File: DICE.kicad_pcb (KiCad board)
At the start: 2 copper layers, 117.3 x 128.5 mm, 116 parts, among them J101 Conn_01x03_Pin, J102 AudioJack2, J103 AudioJack2, J104 AudioJack2, J105 AudioJack2, J106 AudioJack2, J107 AudioJack2, J108 Conn_02x05_Odd_Even, J109 Conn_01x03_Pin, J11 AudioJack2, J110 Conn_01x05_Pin, J111 Conn_01x05_Pin, J112 Conn_01x07_Pin, J113 Conn_01x07_Pin, J114 Conn_01x07_Pin, J115 Conn_01x07_Pin, J116 Conn_01x03_Pin, J117 Conn_01x03_Pin, J2 Conn_01x03_Pin, Q101 BC847, Q102 BC847, SW1 SW_SPDT, SW101 SW_SPDT, SW102 SW_SPDT, U1 TL074, U101 DG412xUE, U102 TL074, U103 TL074

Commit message: Added TRG LED
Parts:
- added ?: , , F.Cu at (115.8, 76.9)
- added D115: LED, LED_THT:LED_D3.0mm, F.Cu at (164.8, 77.0)
- added R132: 4k7, Resistor_SMD:R_1206_3216Metric, B.Cu at (162.7, 73.1)
- C3: value 470n -> 1u
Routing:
- net SAHSWITCH: track 39.1 -> 51.4 mm, vias 2 -> 5
- net Net-(D115-A): track 0.00 -> 4.26 mm
- net NOISERAW: track 67.4 -> 69.4 mm
- net BUFIN: track 42.7 -> 44.2 mm
- net -12V: track 199.6 -> 201.1 mm
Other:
- board text added: "EXT"
- board text added: "INT"
- board text added: "SAH"
- board text added: "TAH"
- board text removed: "IN/NOISE"
- board text removed: "REF INT/EXT"
- board text removed: "SAH/TAH"

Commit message: Added an LED indicator to the COMP output
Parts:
- added ?: , , F.Cu at (115.9, 113.5)
- added D116: LED, LED_THT:LED_D3.0mm, F.Cu at (161.3, 110.4)
- added Q103: BC847, Package_TO_SOT_SMD:SOT-23, B.Cu at (172.6, 122.4)
- added R133: 4k7, Resistor_SMD:R_1206_3216Metric, B.Cu at (172.4, 115.4)
- moved C108 28.9 mm to (161.2, 85.4), turned to 180 degrees
- moved D9 3.38 mm to (162.9, 115.1), turned to 0 degrees
- moved J106 2.96 mm to (167.7, 131.4)
- moved R117 2.96 mm to (157.0, 129.5)
- moved R118 2.96 mm to (157.0, 132.0)
- moved J117 2.96 mm to (173.5, 40.2)
- moved D106 2.96 mm to (163.6, 44.8)
- moved D107 2.96 mm to (163.6, 37.4)
- moved D108 2.96 mm to (156.2, 37.4)
- moved D109 2.96 mm to (156.2, 44.8)
- moved D115 2.96 mm to (162.5, 75.1)
- moved J102 2.96 mm to (167.7, 81.2)
- moved J103 2.96 mm to (154.7, 56.7)
- moved J104 2.96 mm to (154.7, 81.2)
- moved J105 2.96 mm to (167.7, 56.7)
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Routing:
- net COMP: track 47.2 -> 62.5 mm, vias 0 -> 1
- net Net-(D116-A): track 0.00 -> 12.6 mm
- net +12V: track 33.2 -> 44.6 mm
- net Net-(Q103-E): track 0.00 -> 5.08 mm
- net -12V: track 201.1 -> 197.6 mm, vias 5 -> 6
- net Net-(D9-K): track 14.7 -> 12.6 mm
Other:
- outline, holes or cut-outs redrawn

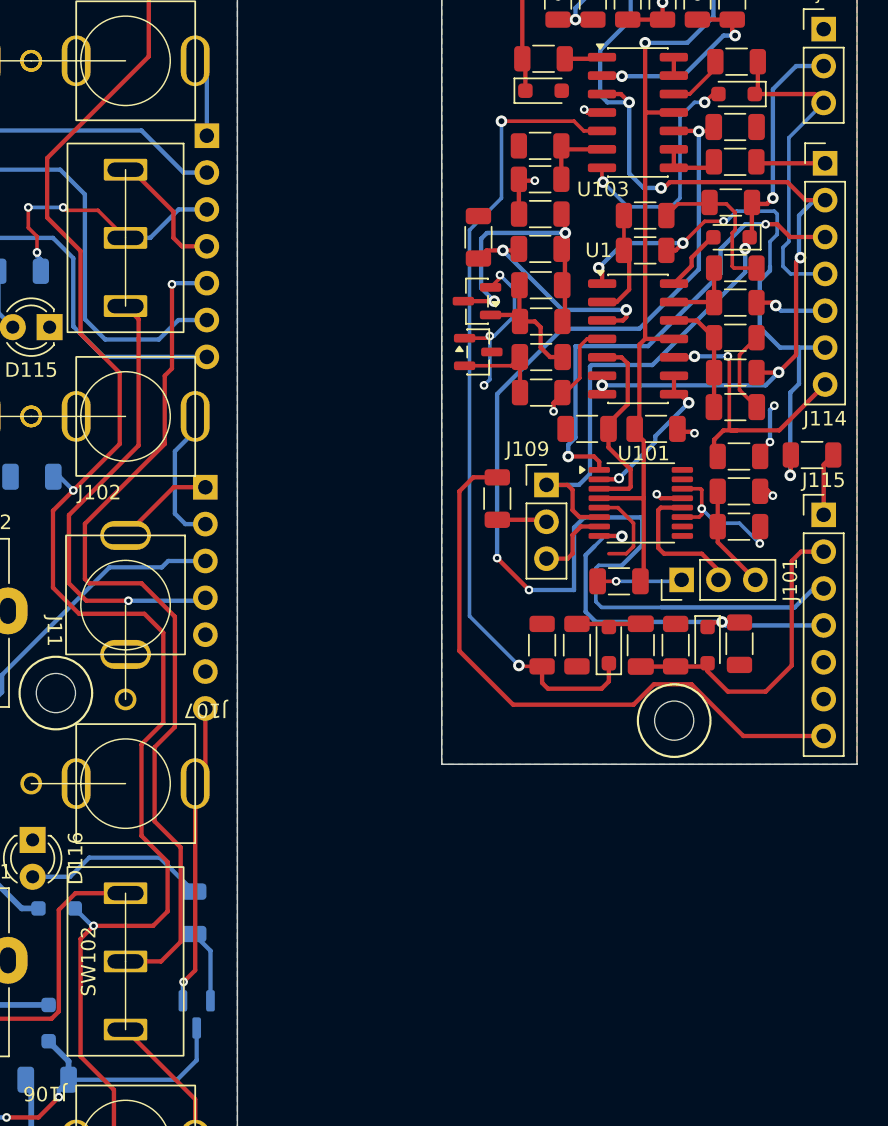
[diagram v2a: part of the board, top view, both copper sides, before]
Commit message: Fixed false positive triggers on COMP output
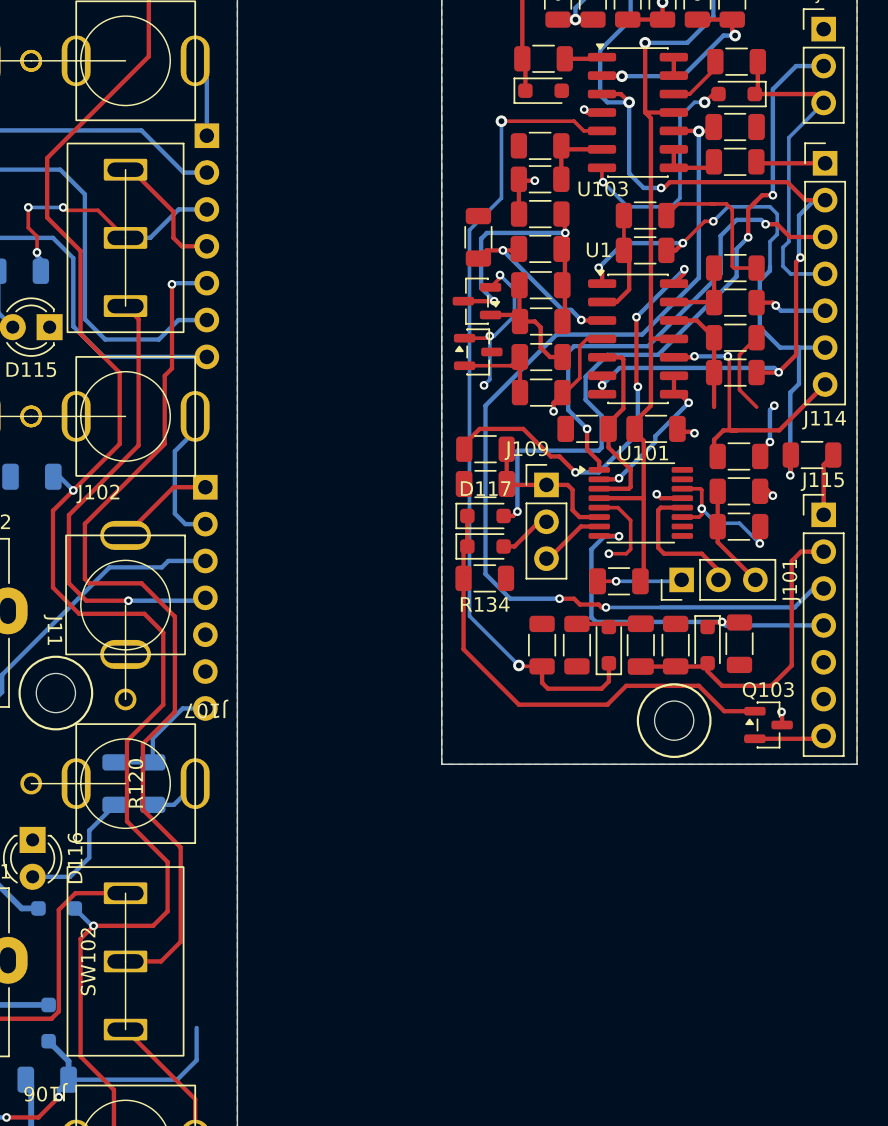
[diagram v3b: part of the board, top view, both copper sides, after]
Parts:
- added D117: 1N4148, Diode_SMD:D_SOD-323_HandSoldering, F.Cu at (192.5, 88.1)
- added R134: 1M, Resistor_SMD:R_1206_3216Metric, F.Cu at (192.4, 92.4)
- Q103: moved to F.Cu
- R119: value 100k -> 47k
- R120: moved to B.Cu
- moved Q103 44.2 mm to (212.0, 102.5), turned to 0 degrees
- moved R120 30.8 mm to (169.6, 106.5), turned to -90 degrees
- moved D104 27.2 mm to (192.5, 90.2), turned to 0 degrees
- moved R119 24.0 mm to (192.5, 83.5)
- moved C101 18.0 mm to (192.5, 85.9), turned to 0 degrees
- moved R133 10.4 mm to (167.0, 106.5), turned to -90 degrees
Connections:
- C101 pad 2: Net-(U1D-+) -> Net-(J109-Pin_1)
- J107 pad T: COMP -> Net-(J107-PadT)
- J109 pad 1: Net-(D104-K) -> Net-(J109-Pin_1)
- J109 pad 2: Net-(J109-Pin_2) -> Net-(D104-A)
- J2 pad 2: Net-(D104-K) -> Net-(D117-A)
- Q103 pad 1: COMP -> Net-(D104-K)
- Q103 pad 2: Net-(Q103-E) -> COMP
- R119 pad 1: GND -> Net-(R119-Pad1)
- R119 pad 2: Net-(D104-K) -> Net-(J109-Pin_1)
- R120 pad 1: Net-(J109-Pin_2) -> COMP
- R120 pad 2: COMP -> Net-(J107-PadT)
- R133 pad 1: Net-(Q103-E) -> COMP
- U1 pad 14: Net-(D104-A) -> Net-(R119-Pad1)
- U101 pad 6: Net-(D104-K) -> Net-(J109-Pin_1)
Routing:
- net Net-(D117-A): track 0.00 -> 48.5 mm, vias 0 -> 3
- net COMP: track 62.5 -> 14.2 mm, vias 1 -> 0
- net Net-(R119-Pad1): track 0.00 -> 29.1 mm, vias 0 -> 4
- net Net-(D104-K): track 46.9 -> 32.2 mm, vias 2 -> 0
- net SLEWPRE: track 104.3 -> 91.0 mm
- net Net-(J109-Pin_1): track 0.00 -> 10.5 mm
- net Net-(Q103-E): track 5.08 -> 0.00 mm
- net Net-(D116-A): track 12.6 -> 8.82 mm
- net Net-(U1A-+): track 15.4 -> 11.8 mm
- net Net-(J107-PadT): track 0.00 -> 3.53 mm
- net Net-(J109-Pin_2): track 3.25 -> 0.00 mm
- net -12V: track 197.6 -> 198.7 mm
- net +12V: track 44.6 -> 45.5 mm, vias 11 -> 12
- net Net-(J109-Pin_3): track 5.32 -> 4.55 mm
- net GATE: track 58.3 -> 57.6 mm
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
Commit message: Add files via upload
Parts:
- J109, J2: moved to B.Cu
- turned J109 to 180 degrees
- turned J2 to 180 degrees
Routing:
- net +12V: track 45.5 -> 33.9 mm
- net Net-(U1D-+): track 8.02 -> 5.66 mm
- net GND: track 104.9 -> 105.9 mm, vias 8 -> 7
- net Net-(D104-A): track 3.65 -> 3.15 mm
